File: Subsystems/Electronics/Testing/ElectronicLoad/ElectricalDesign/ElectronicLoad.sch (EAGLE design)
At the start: 67 parts, among them J1 USB, J2 Current Input, J3 Current Sense, J4 Voltage Sense, J5 SWD, Q1 IRFP4368PBF, Q2 SiRA20DP, Q3 SiRA20DP, Q4 IRFP4368PBF, SW1 Nice Knob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

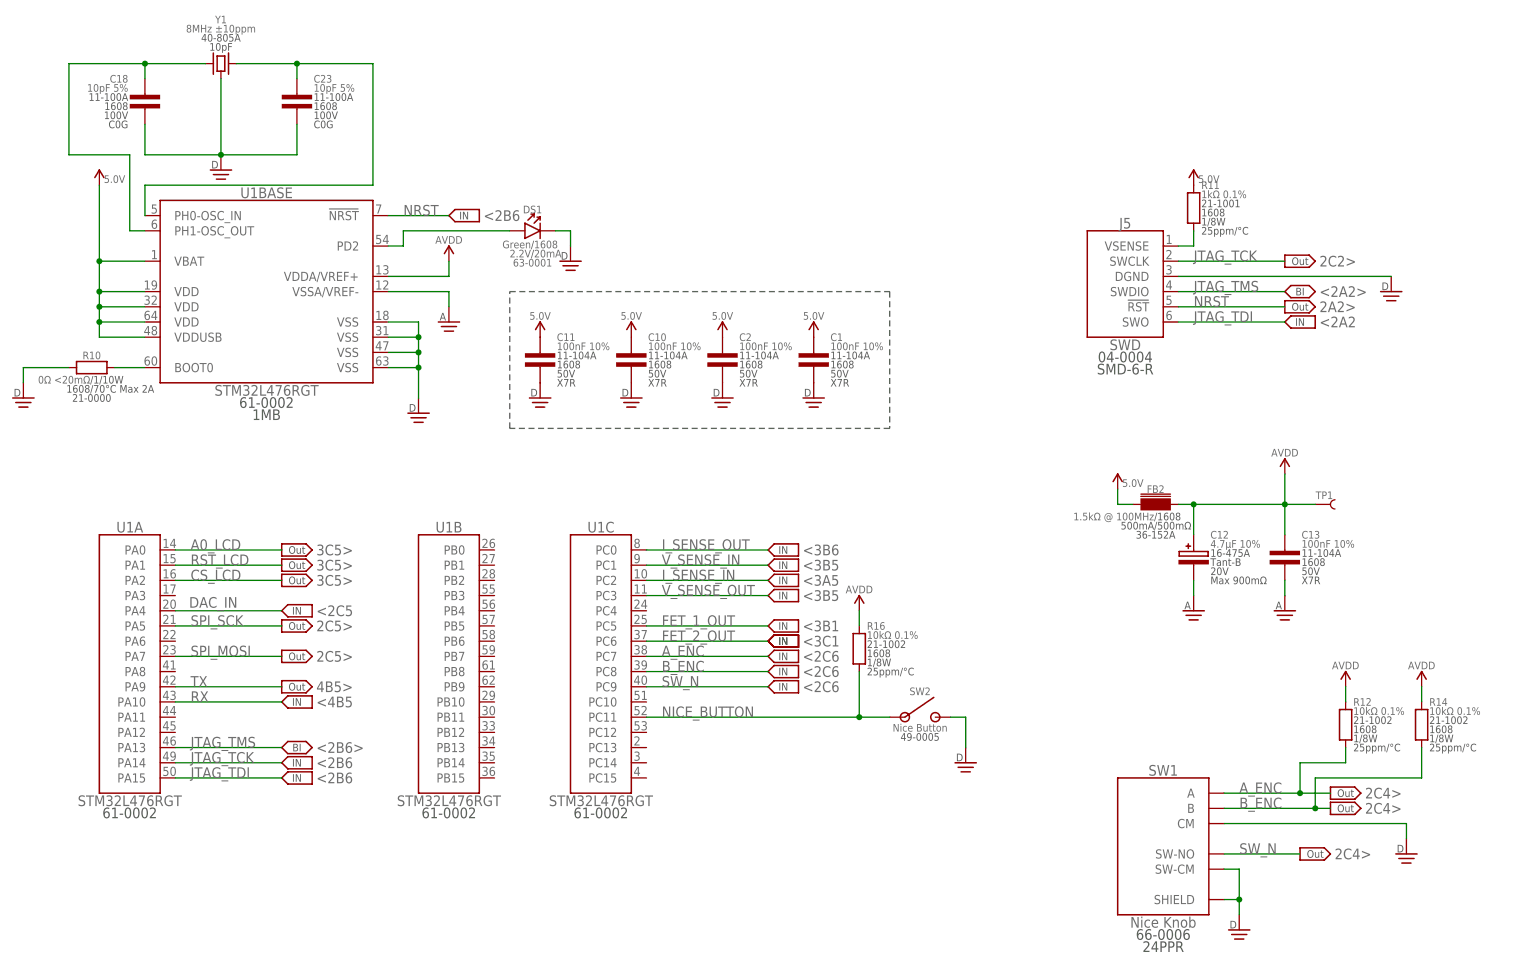
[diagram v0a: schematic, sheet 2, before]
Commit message: Added decapaps, fixed formatting
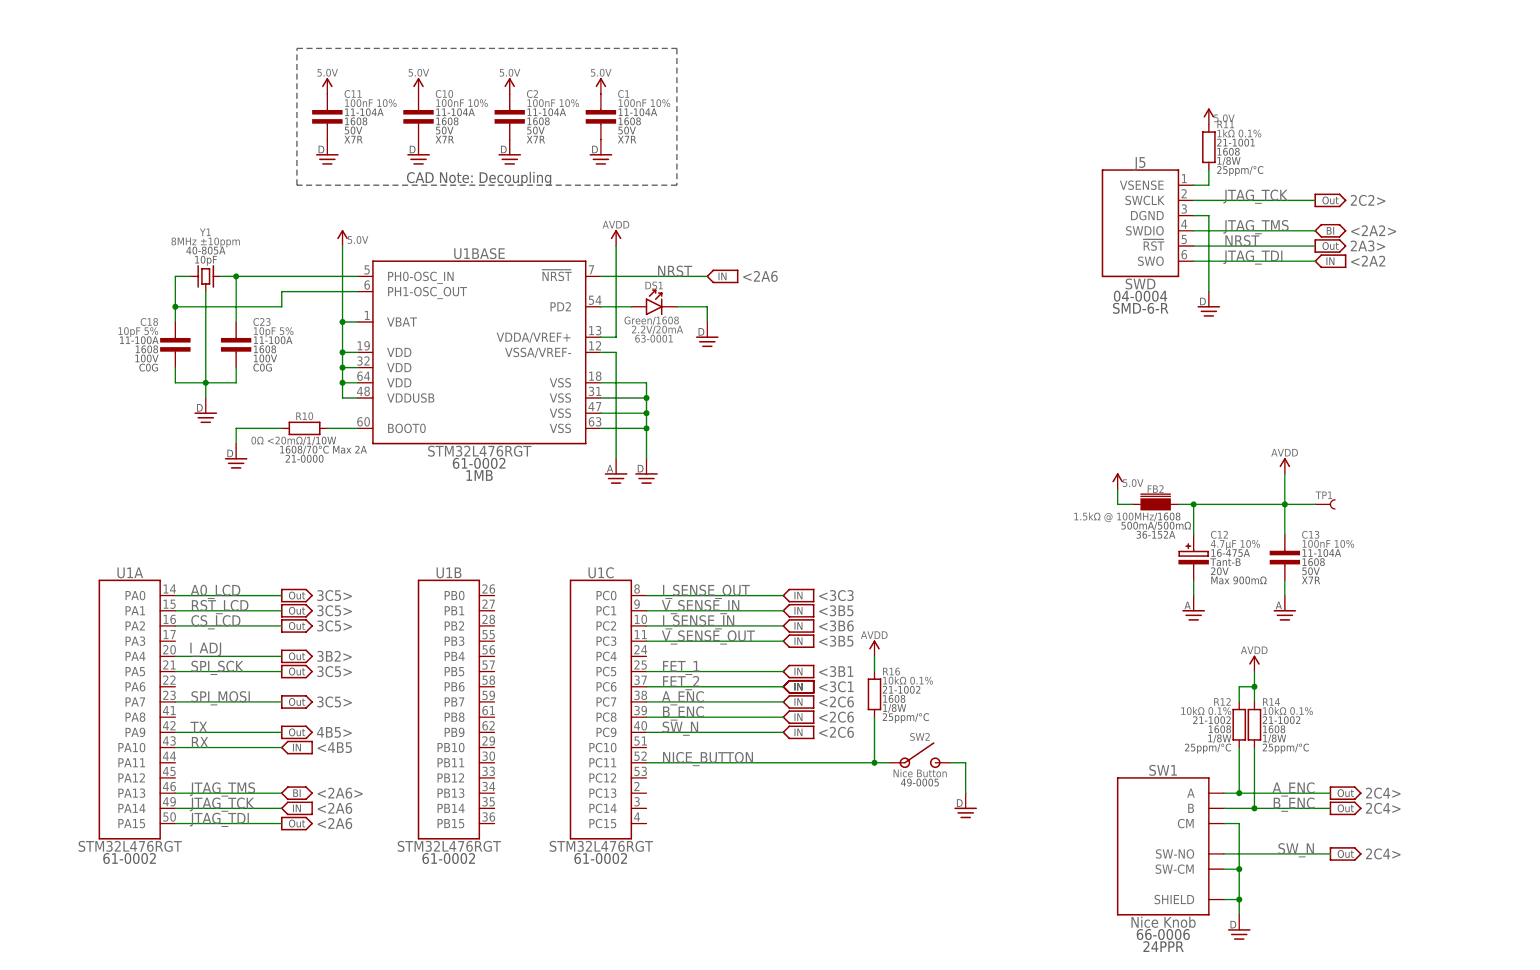
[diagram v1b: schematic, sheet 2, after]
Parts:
- added C24, C25, C26, C27: 100nF 10%, CougsInSpace-Capacitors:CAP-V-100NF-1608
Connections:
- net DAC_IN renamed I_ADJ
- net FET_1_OUT renamed FET_1
- net FET_2_OUT renamed FET_2
- net 5.0V: now also C24.1, C25.1, C26.1
- net AVDD: now also C27.1
- net DGND: now also C24.2, C25.2, C26.2, C27.2
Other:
- note added: "2A3>"
- note added: "3B2>"
- note added: "3B5>"
- note added: "<2A6"
- note added: "<2A6>"
- note added: "<3C3"
- note added: "Page 1: Block Diagram Page 2: Microcontroller Page 3: Electronic Load, LCD Page 4: USB Tranceiver"
- note added: "Page 4"
- note added: "SPI"
- note removed: "1: Overview"
- note removed: "2: Electroic Load Schematic"
- note removed: "2A2>"
- note removed: "2B5>"
- note removed: "2C5>"
- note removed: "3: Microcontroller and USB Schematic"
- note removed: "<2B6"
- note removed: "<2B6>"
- note removed: "<2C5"
- note removed: "<3A5"
- moved on the sheet: B1, C1, C10, C11, C14, C15, C16, C17, C18, C19, C2, C21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

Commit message: Update ElectronicLoad.sch
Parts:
- added J6: (no value), CougsInSpace-Connectors:1X04THT2.54-1X04-LOCK
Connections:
- net DGND: now also J6.1
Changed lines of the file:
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@@
 <?xml version="1.0" encoding="utf-8"?>
 <!DOCTYPE eagle SYSTEM "eagle.dtd">
-<eagle version="9.5.2">
+<eagle version="9.4.2">
 <drawing>
 <settings>
@@
 <setting verticaltext="up"/>
 </settings>
-<grid distance="0.1" unitdist="inch" unit="inch" style="lines" multiple="1" display="no" altdistance="0.05" altunitdist="inch" altunit="inch"/>
+<grid distance="0.1" unitdist="inch" unit="inch" style="lines" multiple="1" display="no" altdistance="0.01" altunitdist="inch" altunit="inch"/>
 <layers>
 <layer number="1" name="Top" color="4" fill="1" visible="no" active="no"/>
@@
 <part name="SUPPLY56" library="CougsInSpace-PowerSymbols" deviceset="5.0V" device=""/>
 <part name="OFFSHEET11" library="CougsInSpace-Aesthetics" deviceset="OFF_SHEET-OUT" device=""/>
+<part name="J6" library="CougsInSpace-Connectors" deviceset="1X04" device="THT2.54-1X04-LOCK"/>
+<part name="SUPPLY66" library="CougsInSpace-PowerSymbols" deviceset="DGND" device=""/>
 </parts>
 <sheets>
@@
 <attribute name="VALUE" x="45.72" y="166.116" size="1.27" layer="96" align="center"/>
 </instance>
+<instance part="J6" gate="G$1" x="73.66" y="157.48" smashed="yes">
+<attribute name="VALUE" x="74.295" y="151.13" size="1.778" layer="96" align="center"/>
+<attribute name="NAME" x="74.295" y="166.37" size="1.778" layer="95" align="center"/>
+<attribute name="SKU" x="74.295" y="149.098" size="1.778" layer="97" align="center"/>
+<attribute name="PACKAGE" x="74.295" y="147.066" size="1.778" layer="97" align="center"/>
+</instance>
+<instance part="SUPPLY66" gate="1" x="83.82" y="162.56" smashed="yes" rot="R90"/>
 </instances>
 <busses>
@@
 <pinref part="SUPPLY65" gate="1" pin="DGND"/>
 </segment>
-</net>
+<segment>
+<pinref part="J6" gate="G$1" pin="1"/>
+<pinref part="SUPPLY66" gate="1" pin="DGND"/>
+</segment>
+</net>

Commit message: Update ElectronicLoad.sch
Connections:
- new net FAN_CONTROL: J6.4
- new net FAN_DC: J6.2
- new net FAN_GND: J6.1
- new net FAN_SENSE: J6.3
- new net N$2: U1A.PA11
- net DGND: no longer J6.1
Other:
- note added: "3A2>"
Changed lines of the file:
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@@
 <part name="J6" library="CougsInSpace-Connectors" deviceset="1X04" device="THT2.54-1X04-LOCK"/>
 <part name="SUPPLY66" library="CougsInSpace-PowerSymbols" deviceset="DGND" device=""/>
+<part name="OFFSHEET47" library="CougsInSpace-Aesthetics" deviceset="OFF_SHEET-OUT" device=""/>
+<part name="OFFSHEET49" library="CougsInSpace-Aesthetics" deviceset="OFF_SHEET-IN" device=""/>
+<part name="OFFSHEET50" library="CougsInSpace-Aesthetics" deviceset="OFF_SHEET-IN" device=""/>
+<part name="OFFSHEET51" library="CougsInSpace-Aesthetics" deviceset="OFF_SHEET-IN" device=""/>
 </parts>
 <sheets>
@@
 <wire x1="53.34" y1="162.56" x2="53.34" y2="185.42" width="0.1524" layer="97" style="shortdash"/>
 <text x="83.82" y="163.83" size="1.778" layer="97" align="center">CAD Note: Decoupling</text>
+<text x="55.88" y="66.04" size="1.778" layer="95" align="center-left"> 3A2&gt;</text>
 </plain>
 <instances>
@@
 <instance part="OFFSHEET25" gate="G$1" x="53.34" y="83.82" smashed="yes" rot="MR0"/>
 <instance part="OFFSHEET11" gate="G$1" x="53.34" y="55.88" smashed="yes" rot="MR0"/>
+<instance part="OFFSHEET47" gate="G$1" x="53.34" y="66.04" smashed="yes" rot="MR0"/>
 </instances>
 <busses>
@@
 <wire x1="43.18" y1="139.7" x2="43.18" y2="147.32" width="0.1524" layer="91"/>
 <junction x="43.18" y="147.32"/>
+</segment>
+</net>
+<net name="N$2" class="0">
+<segment>
+<pinref part="U1" gate="A" pin="PA11"/>
+<wire x1="33.02" y1="66.04" x2="50.8" y2="66.04" width="0.1524" layer="91"/>
+</segment>
+</net>
+<net name="FAN_SENSE" class="0">
+<segment>
+<wire x1="33.02" y1="66.04" x2="50.8" y2="66.04" width="0.1524" layer="91"/>
+<label x="35.56" y="66.04" size="1.778" layer="95"/>
+<label x="35.56" y="66.04" size="1.778" layer="95"/>
 </segment>
 </net>
@@
 <wire x1="149.86" y1="53.34" x2="175.26" y2="53.34" width="0.1524" layer="97" style="shortdash"/>
 <text x="162.56" y="34.29" size="1.778" layer="97" align="center">CAD Note: Decoupling</text>
+<text x="106.68" y="157.48" size="1.778" layer="95" align="center-left"> &lt;2C2</text>
+<text x="106.68" y="154.94" size="1.778" layer="95" align="center-left"> &lt;2C2</text>
+<text x="106.68" y="160.02" size="1.778" layer="95" align="center-left"> &lt;2C2</text>
 </plain>
 <instances>
@@
 <attribute name="PACKAGE" x="74.295" y="147.066" size="1.778" layer="97" align="center"/>
 </instance>
-<instance part="SUPPLY66" gate="1" x="83.82" y="162.56" smashed="yes" rot="R90"/>
+<instance part="SUPPLY66" gate="1" x="104.14" y="162.56" smashed="yes" rot="R90"/>
+<instance part="OFFSHEET49" gate="G$1" x="104.14" y="157.48" smashed="yes" rot="MR0"/>
+<instance part="OFFSHEET50" gate="G$1" x="104.14" y="154.94" smashed="yes" rot="MR0"/>
+<instance part="OFFSHEET51" gate="G$1" x="104.14" y="160.02" smashed="yes" rot="MR0"/>
 </instances>
 <busses>
@@
 <pinref part="C27" gate="G$1" pin="2"/>
 <pinref part="SUPPLY65" gate="1" pin="DGND"/>
-</segment>
-<segment>
-<pinref part="J6" gate="G$1" pin="1"/>
-<pinref part="SUPPLY66" gate="1" pin="DGND"/>
 </segment>
 </net>
@@
 </segment>
 </net>
+<net name="FAN_SENSE" class="0">
+<segment>
+<pinref part="J6" gate="G$1" pin="3"/>
+<wire x1="81.28" y1="157.48" x2="101.6" y2="157.48" width="0.1524" layer="91"/>
+<label x="83.82" y="157.48" size="1.778" layer="95"/>
+</segment>
+</net>
+<net name="FAN_CONTROL" class="0">
+<segment>
+<pinref part="J6" gate="G$1" pin="4"/>
+<wire x1="81.28" y1="154.94" x2="101.6" y2="154.94" width="0.1524" layer="91"/>
+<label x="83.82" y="154.94" size="1.778" layer="95"/>
+</segment>
+</net>
+<net name="FAN_SENSE1" class="0">
+<segment>
+<wire x1="81.28" y1="154.94" x2="101.6" y2="154.94" width="0.1524" layer="91"/>
+</segment>
+</net>
+<net name="FAN_DC" class="0">
+<segment>
+<pinref part="J6" gate="G$1" pin="2"/>
+<wire x1="81.28" y1="160.02" x2="101.6" y2="160.02" width="0.1524" layer="91"/>
+<label x="83.82" y="160.02" size="1.778" layer="95"/>
+</segment>
+</net>
+<net name="FAN_GND" class="0">
+<segment>
+<pinref part="J6" gate="G$1" pin="1"/>
+<pinref part="SUPPLY66" gate="1" pin="DGND"/>
+<wire x1="101.6" y1="162.56" x2="81.28" y2="162.56" width="0.1524" layer="91"/>
+<label x="83.82" y="162.56" size="1.778" layer="95"/>
+</segment>
+</net>
